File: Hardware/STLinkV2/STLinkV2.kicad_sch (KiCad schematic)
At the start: 63 parts, among them J1 USB_B_Micro, J2 SWD, J3 ISP, J4 RS232, J5 JTAG, U1 STM32F103CBT6, U2 SRV05-4, U3 HT7833, U4 SRV05-4, U5 SRV05-4, U6 74AVCH2T45DC,125, U7 74AVCH2T45DC,125, Y1 8MHz

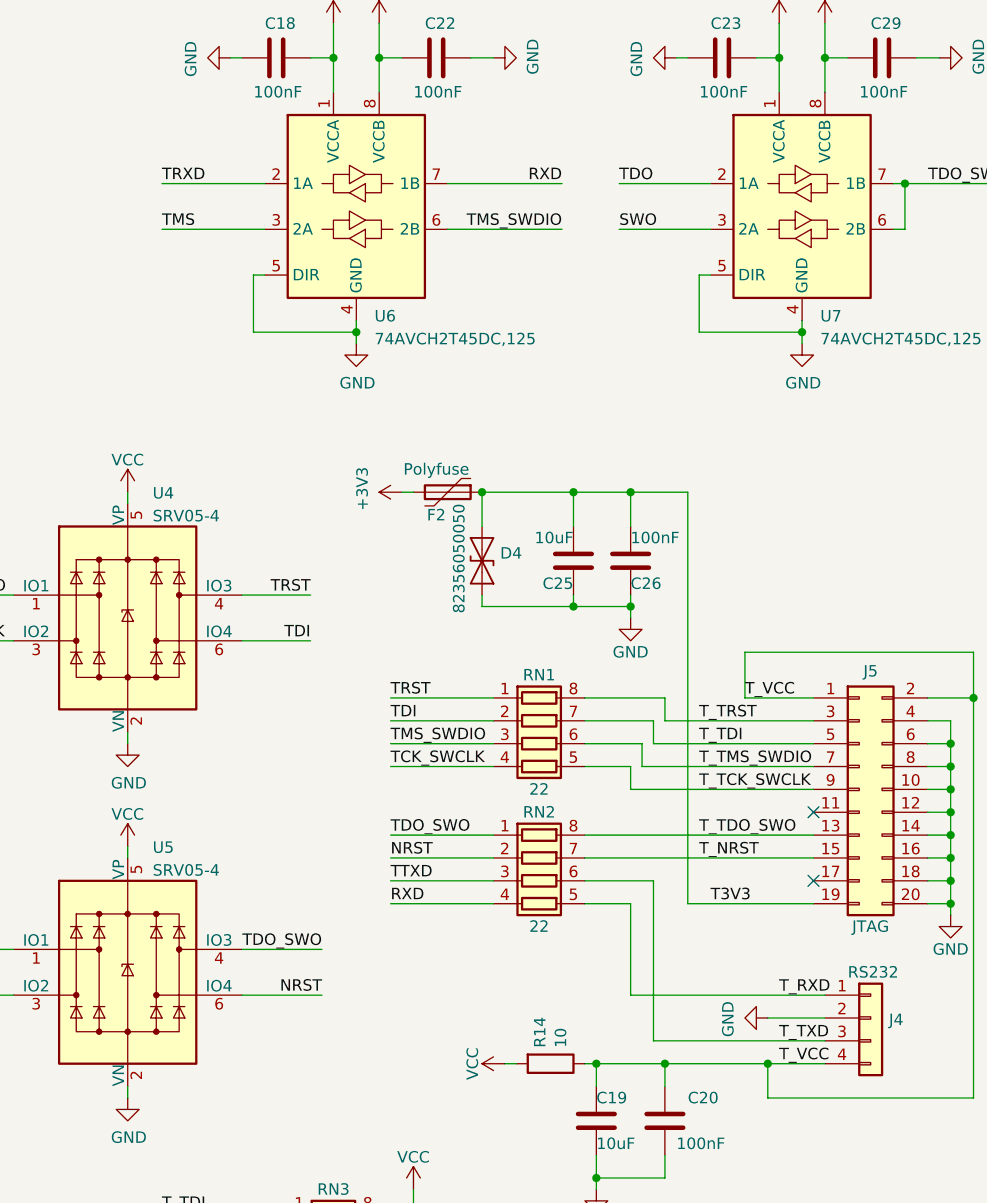
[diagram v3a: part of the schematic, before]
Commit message: STLink V2 hardware review
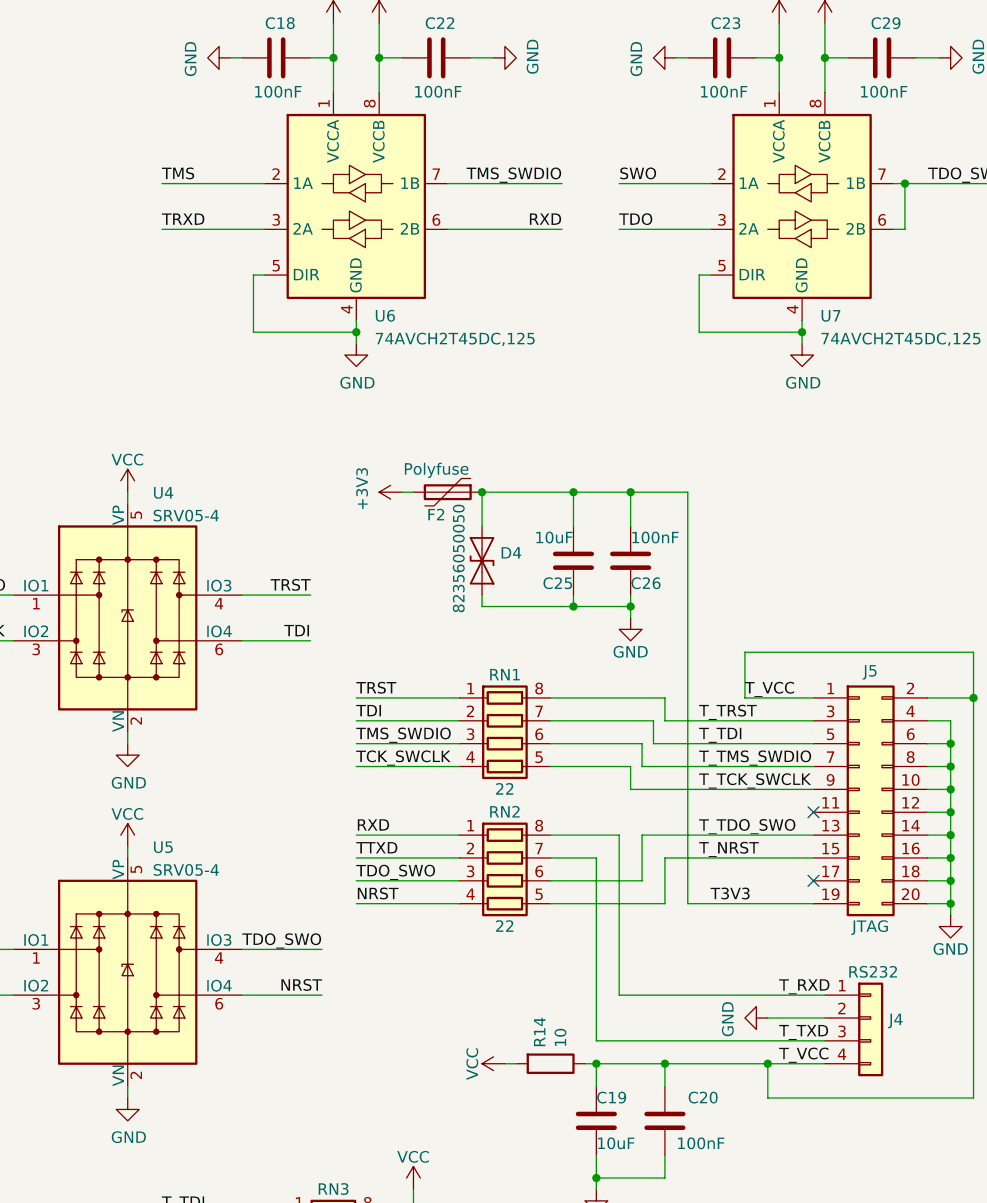
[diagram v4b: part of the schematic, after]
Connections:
- net NRST: now also RN2.4 (R4.1); no longer RN2.2 (R2.1)
- net RXD: now also RN2.1 (R1.1), U6.6 (2B); no longer RN2.4 (R4.1), U6.7 (1B)
- net SWO: now also U7.2 (1A); no longer U7.3 (2A)
- net TDO: now also U7.3 (2A); no longer U7.2 (1A)
- net TDO_SWO: now also RN2.3 (R3.1); no longer RN2.1 (R1.1)
- net TMS: now also U6.2 (1A); no longer U6.3 (2A)
- net TMS_SWDIO: now also U6.7 (1B); no longer U6.6 (2B)
- net TRXD: now also U6.3 (2A); no longer U6.2 (1A)
- net TTXD: now also RN2.2 (R2.1); no longer RN2.3 (R3.1)
- net T_NRST: now also RN2.5 (R4.2); no longer RN2.7 (R2.2)
- net T_RXD: now also RN2.8 (R1.2); no longer RN2.5 (R4.2)
- net T_TDO_SWO: now also RN2.6 (R3.2); no longer RN2.8 (R1.2)
- net T_TXD: now also RN2.7 (R2.2); no longer RN2.6 (R3.2)
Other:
- moved on the sheet: RN1, RN2

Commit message: ^STLink V2 Hardware review.
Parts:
- removed D4: 82356050050, Diode_SMD:D_0603_1608Metric, symbol Diode:ESD9B5.0ST5G
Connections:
- net +3V3: now also U5.5 (VP)
- net NRST: now also U5.1 (IO1); no longer U5.6 (IO4)
- net RXD: now also RN2.8 (R1.2), U5.6 (IO4); no longer RN2.1 (R1.1), U5.3 (IO2)
- net TDO_SWO: now also U5.3 (IO2); no longer U5.4 (IO3)
- net TTXD: now also RN2.7 (R2.2), U5.4 (IO3); no longer RN2.2 (R2.1), U5.1 (IO1)
- net T_RXD: now also RN2.1 (R1.1); no longer RN2.8 (R1.2)
- net T_TXD: now also RN2.2 (R2.1); no longer RN2.7 (R2.2)
- net VCC: no longer U5.5 (VP)
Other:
- moved on the sheet: F2

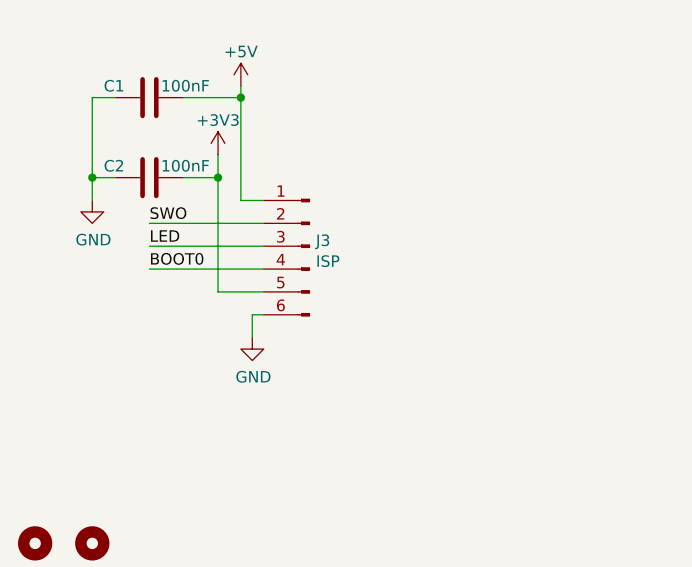
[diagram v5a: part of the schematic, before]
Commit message: STLink V2 hardware review
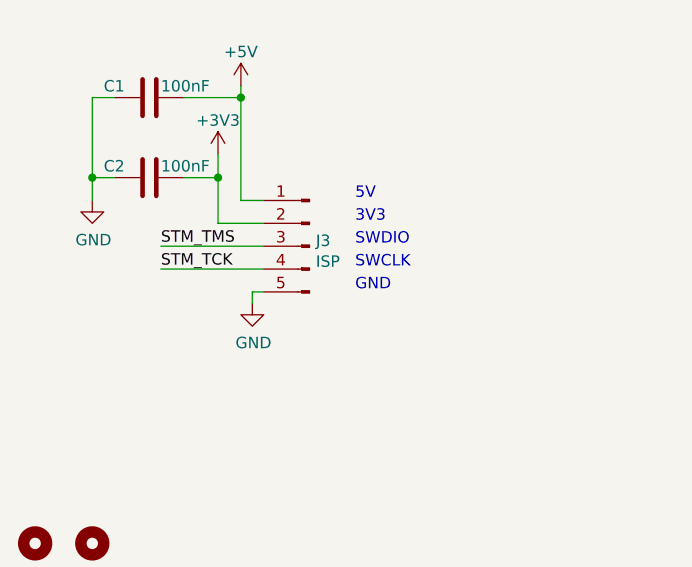
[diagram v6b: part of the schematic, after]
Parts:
- J3: footprint Connector_PinHeader_2.54mm:PinHeader_1x06_P2.54mm_Vertical -> Connector_PinHeader_2.54mm:PinHeader_1x05_P2.54mm_Vertical; symbol Connector:Conn_01x06_Male -> Connector:Conn_01x05_Male
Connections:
- net +3V3: now also J3.2 (Pin_2); no longer J3.5 (Pin_5)
- net BOOT0: no longer J3.4 (Pin_4)
- net GND: now also J3.5 (Pin_5); no longer J3.6 (Pin_6)
- net LED: no longer J3.3 (Pin_3)
- net STM_TCK: now also J3.4 (Pin_4)
- net STM_TMS: now also J3.3 (Pin_3)
- net SWO: no longer J3.2 (Pin_2)
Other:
- note added: "3V3"
- note added: "5V"
- note added: "GND"
- note added: "SWCLK"
- note added: "SWDIO"
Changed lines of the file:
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@@
   (title_block
     (title "STLink-V2")
-    (date "2022-11-20")
+    (date "2022-11-24")
     (rev "1")
     (company "Mathias Gruber")
@@
   (junction (at 358.14 137.16) (diameter 0) (color 0 0 0 0)
   )
-  (junction (at 35.56 240.03) (diameter 0) (color 0 0 0 0)
-  )
   (junction (at 320.04 127) (diameter 0) (color 0 0 0 0)
   )
@@
   (junction (at 355.6 144.78) (diameter 0) (color 0 0 0 0)
   )
+  (junction (at 35.56 240.03) (diameter 0) (color 0 0 0 0)
+  )
   (junction (at 144.78 118.11) (diameter 0) (color 0 0 0 0)
   )
@@
     (stroke (width 0) (type default) (color 0 0 0 0))
   )
-  (wire (pts (xy 40.64 245.11) (xy 27.94 245.11))
+  (wire (pts (xy 40.64 247.65) (xy 29.21 247.65))
     (stroke (width 0) (type default) (color 0 0 0 0))
   )
@@
     (stroke (width 0) (type default) (color 0 0 0 0))
   )
+  (wire (pts (xy 40.64 245.11) (xy 35.56 245.11))
+    (stroke (width 0) (type default) (color 0 0 0 0))
+  )
   (wire (pts (xy 350.52 85.09) (xy 350.52 80.01))
     (stroke (width 0) (type default) (color 0 0 0 0))
@@
     (stroke (width 0) (type default) (color 0 0 0 0))
   )
+  (wire (pts (xy 35.56 240.03) (xy 35.56 245.11))
+    (stroke (width 0) (type default) (color 0 0 0 0))
+  )
   (wire (pts (xy 279.4 90.17) (xy 278.13 90.17))
     (stroke (width 0) (type default) (color 0 0 0 0))
@@
     (stroke (width 0) (type default) (color 0 0 0 0))
   )
-  (wire (pts (xy 40.64 247.65) (xy 27.94 247.65))
+  (wire (pts (xy 40.64 250.19) (xy 29.21 250.19))
     (stroke (width 0) (type default) (color 0 0 0 0))
   )
@@
     (stroke (width 0) (type default) (color 0 0 0 0))
   )
-  (wire (pts (xy 40.64 250.19) (xy 27.94 250.19))
-    (stroke (width 0) (type default) (color 0 0 0 0))
-  )
   (wire (pts (xy 76.2 106.68) (xy 76.2 110.49))
     (stroke (width 0) (type default) (color 0 0 0 0))
@@
     (stroke (width 0) (type default) (color 0 0 0 0))
   )
-  (wire (pts (xy 35.56 252.73) (xy 35.56 240.03))
-    (stroke (width 0) (type default) (color 0 0 0 0))
-  )
   (wire (pts (xy 351.79 66.04) (xy 354.33 66.04))
     (stroke (width 0) (type default) (color 0 0 0 0))
@@
     (stroke (width 0) (type default) (color 0 0 0 0))
   )
-  (wire (pts (xy 40.64 252.73) (xy 35.56 252.73))
-    (stroke (width 0) (type default) (color 0 0 0 0))
-  )
   (wire (pts (xy 242.57 170.18) (xy 251.46 170.18))
     (stroke (width 0) (type default) (color 0 0 0 0))
@@
     (stroke (width 0) (type default) (color 0 0 0 0))
   )
-  (wire (pts (xy 39.37 255.27) (xy 39.37 257.81))
+  (wire (pts (xy 39.37 252.73) (xy 39.37 254))
     (stroke (width 0) (type default) (color 0 0 0 0))
   )
@@
     (stroke (width 0) (type default) (color 0 0 0 0))
   )
-  (wire (pts (xy 40.64 255.27) (xy 39.37 255.27))
+  (wire (pts (xy 40.64 252.73) (xy 39.37 252.73))
     (stroke (width 0) (type default) (color 0 0 0 0))
   )
@@
     (stroke (width 0) (type default) (color 0 0 0 0))
   )
-  (label "SWO" (at 27.94 245.11 0)
+  (text "GND" (at 50.8 252.73 0)
+    (effects (font (size 1.27 1.27)) (justify left bottom))
+  )
+  (text "SWCLK" (at 50.8 250.19 0)
+    (effects (font (size 1.27 1.27)) (justify left bottom))
+  )
+  (text "5V" (at 50.8 242.57 0)
+    (effects (font (size 1.27 1.27)) (justify left bottom))
+  )
+  (text "SWDIO" (at 50.8 247.65 0)
+    (effects (font (size 1.27 1.27)) (justify left bottom))
+  )
+  (text "3V3" (at 50.8 245.11 0)
     (effects (font (size 1.27 1.27)) (justify left bottom))
   )
@@
     (effects (font (size 1.27 1.27)) (justify right bottom))
   )
-  (label "LED" (at 27.94 247.65 0)
-    (effects (font (size 1.27 1.27)) (justify left bottom))
-  )
   (label "TRST" (at 284.48 125.73 180)
     (effects (font (size 1.27 1.27)) (justify right bottom))
@@
     (effects (font (size 1.27 1.27)) (justify left bottom))
   )
-  (label "BOOT0" (at 27.94 250.19 0)
-    (effects (font (size 1.27 1.27)) (justify left bottom))
-  )
   (label "OSC_OUT" (at 158.75 172.72 90)
     (effects (font (size 1.27 1.27)) (justify left bottom))
@@
     (effects (font (size 1.27 1.27)) (justify right bottom))
   )
+  (label "STM_TCK" (at 29.21 250.19 0)
+    (effects (font (size 1.27 1.27)) (justify left bottom))
+  )
   (label "TMS" (at 80.01 210.82 0)
     (effects (font (size 1.27 1.27)) (justify left bottom))
@@
     (effects (font (size 1.27 1.27)) (justify left bottom))
   )
+  (label "STM_TMS" (at 29.21 247.65 0)
+    (effects (font (size 1.27 1.27)) (justify left bottom))
+  )
   (label "TCK_SWCLK" (at 240.03 130.81 0)
     (effects (font (size 1.27 1.27)) (justify left bottom))
@@
     (pin "2")
   )
-  (symbol (lib_id "Connector:Conn_01x06_Male") (at 45.72 247.65 0) (mirror y) (unit 1)
+  (symbol (lib_id "Connector:Conn_01x05_Male") (at 45.72 247.65 0) (mirror y) (unit 1)
     (in_bom yes) (on_board yes)
     (property "Reference" "J3" (id 0) (at 46.4312 247.0404 0)
@@
       (effects (font (size 1.27 1.27)) (justify right))
     )
-    (property "Footprint" "Connector_PinHeader_2.54mm:PinHeader_1x06_P2.54mm_Vertical" (id 2) (at 45.72 247.65 0)
+    (property "Footprint" "Connector_PinHeader_2.54mm:PinHeader_1x05_P2.54mm_Vertical" (id 2) (at 45.72 247.65 0)
       (effects (font (size 1.27 1.27)) hide)
     )
@@
     (pin "4")
     (pin "5")
-    (pin "6")
   )
-  (symbol (lib_id "power:GND") (at 39.37 257.81 0) (unit 1)
+  (symbol (lib_id "power:GND") (at 39.37 254 0) (unit 1)
     (in_bom yes) (on_board yes)
-    (property "Reference" "#PWR09" (id 0) (at 39.37 264.16 0)
+    (property "Reference" "#PWR09" (id 0) (at 39.37 260.35 0)
       (effects (font (size 1.27 1.27)) hide)
     )
-    (property "Value" "GND" (id 1) (at 39.497 262.2042 0))
-    (property "Footprint" "" (id 2) (at 39.37 257.81 0)
+    (property "Value" "GND" (id 1) (at 39.497 258.3942 0))
+    (property "Footprint" "" (id 2) (at 39.37 254 0)
       (effects (font (size 1.27 1.27)) hide)
     )
-    (property "Datasheet" "" (id 3) (at 39.37 257.81 0)
+    (property "Datasheet" "" (id 3) (at 39.37 254 0)
       (effects (font (size 1.27 1.27)) hide)
     )
@@
     )
     (path "/00000000-0000-0000-0000-0000611f3006"
-      (reference "J3") (unit 1) (value "ISP") (footprint "Connector_PinHeader_2.54mm:PinHeader_1x06_P2.54mm_Vertical")
+      (reference "J3") (unit 1) (value "ISP") (footprint "Connector_PinHeader_2.54mm:PinHeader_1x05_P2.54mm_Vertical")
     )
     (path "/e671cbaf-1558-41de-b94b-e049264f8723"

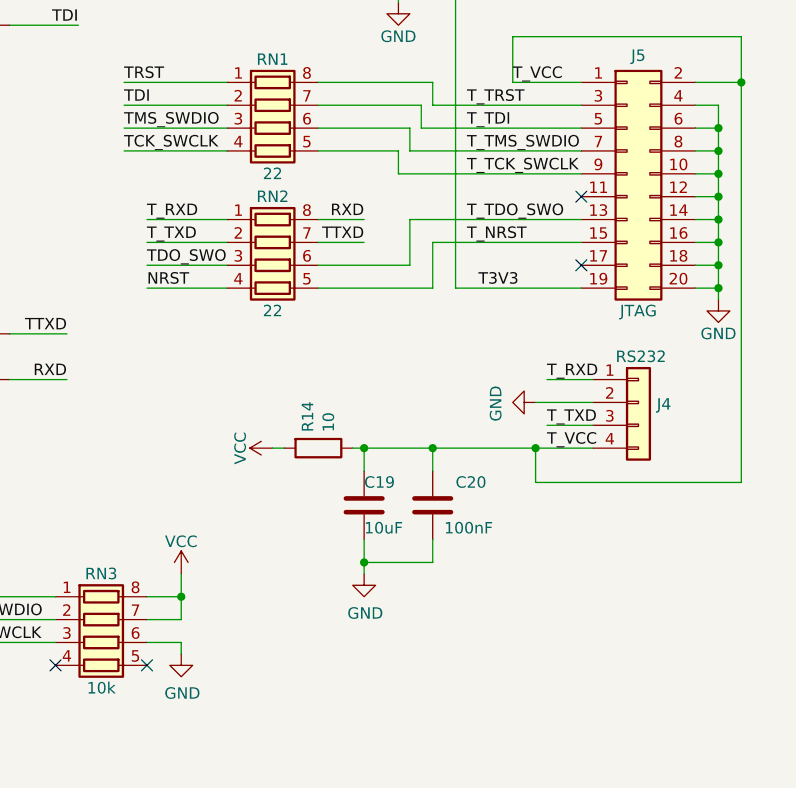
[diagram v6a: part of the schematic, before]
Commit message: Minor tweaks on VCC (ref)
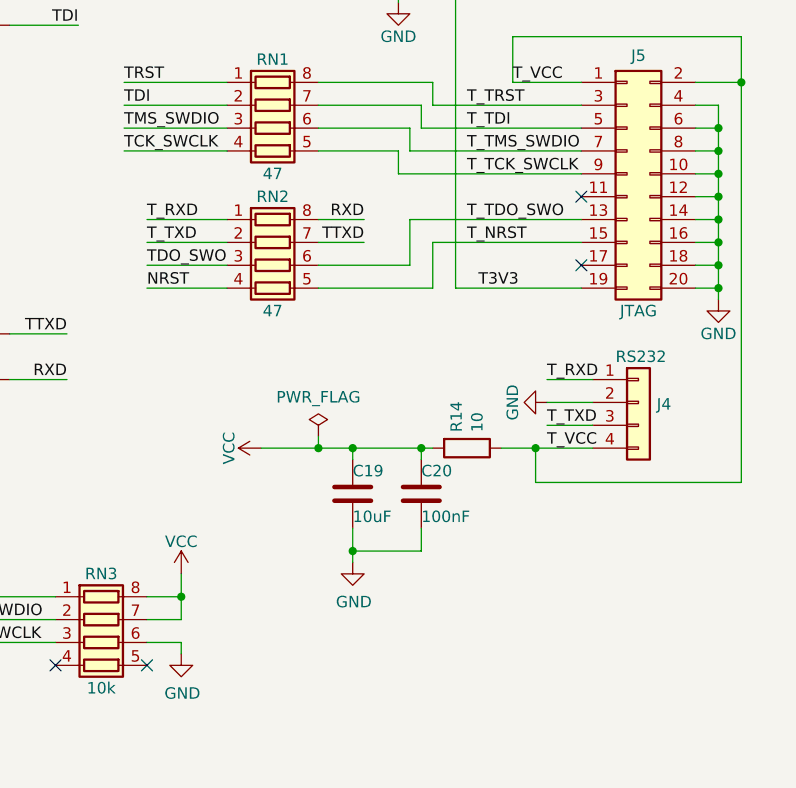
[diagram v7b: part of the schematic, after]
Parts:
- RN1, RN2: value 22 -> 47
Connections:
- net T_VCC: no longer C19.1, C20.1
- net VCC: now also C19.1, C20.1
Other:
- moved on the sheet: C19, C20, R14
